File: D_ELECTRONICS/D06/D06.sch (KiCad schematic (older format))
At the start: 9 parts, among them J4 Conn_01x02_Female, J5 Conn_01x02_Female, Q1 BSS138

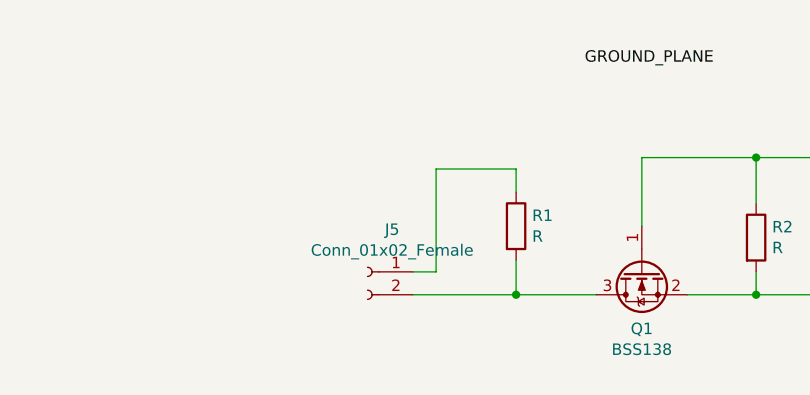
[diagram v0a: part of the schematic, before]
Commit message: fixed signal trace
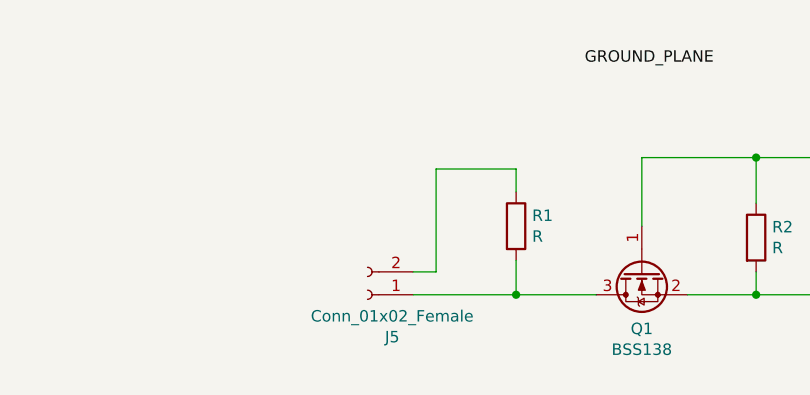
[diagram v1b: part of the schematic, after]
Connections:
- net at Q1.3 (D), R1.2: now also J5.1 (Pin_1); no longer J5.2 (Pin_2)
- net at R1.1: now also J5.2 (Pin_2); no longer J5.1 (Pin_1)
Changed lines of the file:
@@
 L Connector:Conn_01x02_Female J5
 U 1 1 5F8A503D
-P 5300 2550
-F 0 "J5" H 5192 2735 50  0000 C CNN
-F 1 "Conn_01x02_Female" H 5192 2644 50  0000 C CNN
-F 2 "TerminalBlock_4Ucon:TerminalBlock_4Ucon_1x02_P3.50mm_Horizontal" H 5300 2550 50  0001 C CNN
-F 3 "~" H 5300 2550 50  0001 C CNN
-	1    5300 2550
-	-1   0    0    -1
+P 5300 2650
+F 0 "J5" H 5192 2835 50  0000 C CNN
+F 1 "Conn_01x02_Female" H 5192 2744 50  0000 C CNN
+F 2 "TerminalBlock_4Ucon:TerminalBlock_4Ucon_1x02_P3.50mm_Horizontal" H 5300 2650 50  0001 C CNN
+F 3 "~" H 5300 2650 50  0001 C CNN
+	1    5300 2650
+	-1   0    0    1
 $EndComp
 $Comp
@@
 	7000 2050 7250 2050
 Wire Wire Line
-	5500 2550 5600 2550
-Wire Wire Line
 	5600 2550 5600 2100
 Wire Wire Line
 	5600 2100 5950 2100
 Wire Wire Line
-	5500 2650 5950 2650
+	5500 2550 5600 2550
+Wire Wire Line
+	5950 2650 5500 2650
 Connection ~ 5950 2650
 $EndSCHEMATC
